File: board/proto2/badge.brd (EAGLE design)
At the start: 160 x 100 mm, 59 parts, among them IC1 TLV62569, J1 5051101092

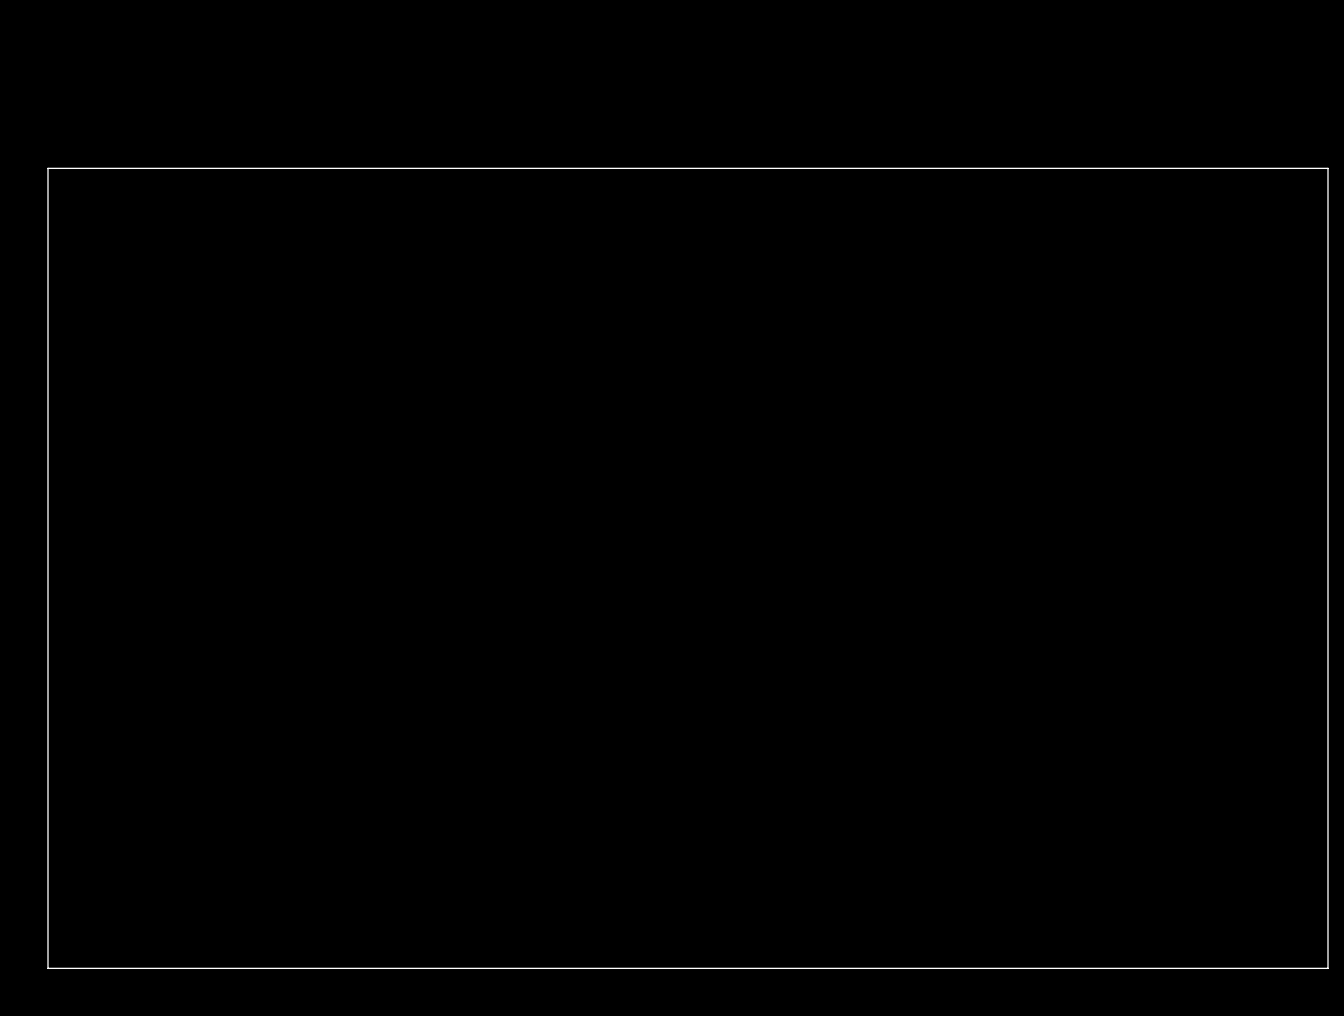
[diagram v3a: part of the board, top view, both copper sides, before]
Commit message: adding outline of monkey to PCB
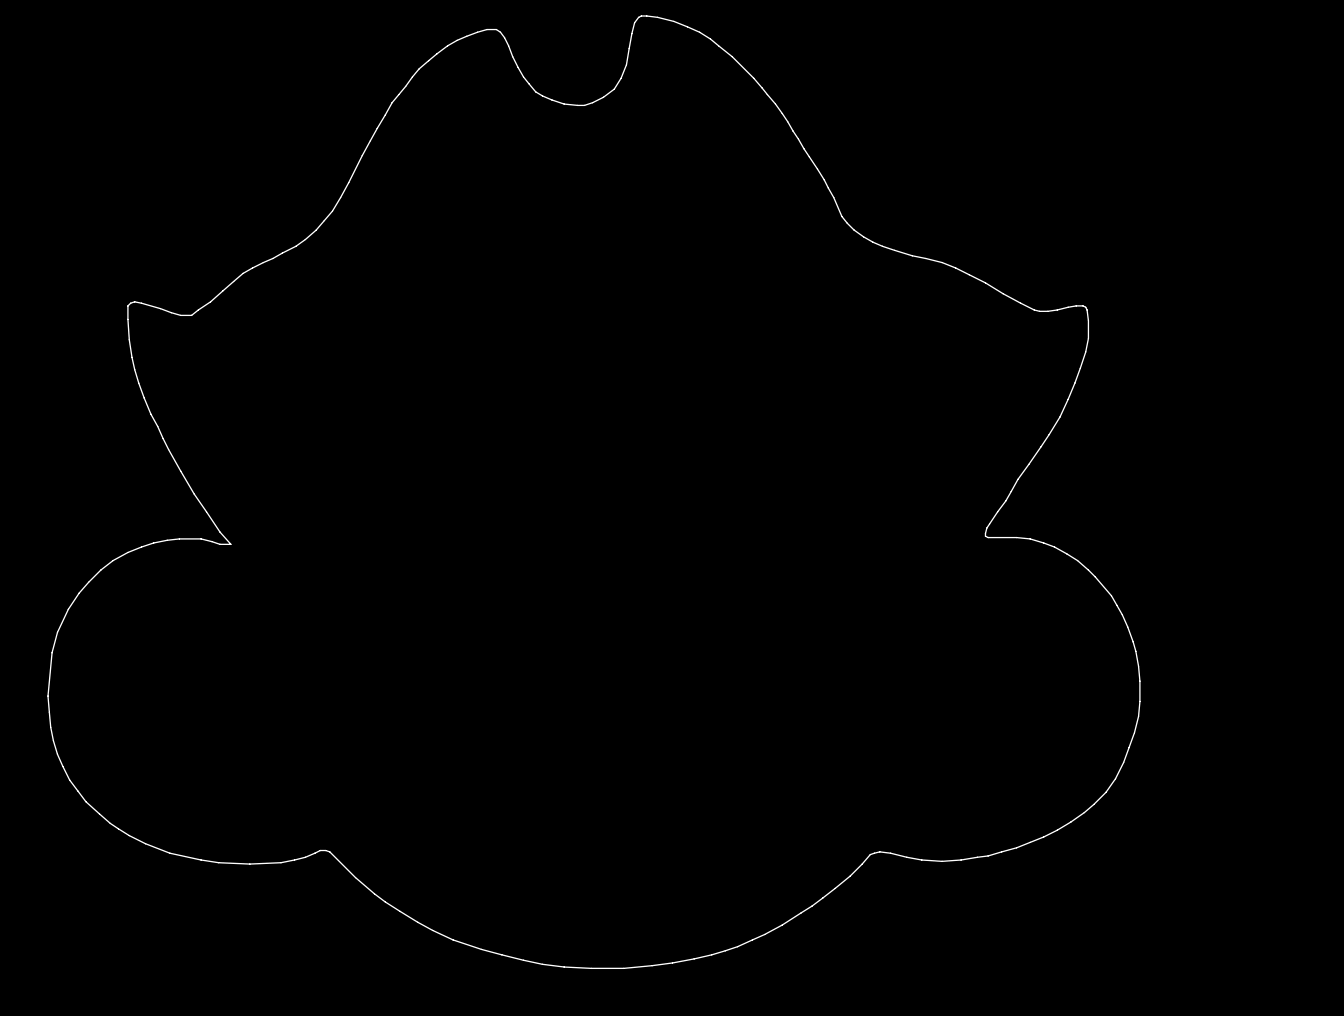
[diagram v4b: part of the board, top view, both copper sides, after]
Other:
- board size 160 x 100 mm -> 136.5 x 119 mm
